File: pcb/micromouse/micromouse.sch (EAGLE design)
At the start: 55 parts, among them J1 Connector_M1, J2 Connector_M1, J4 Programmer, T1 2N3904

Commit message: Add correct switch, change connection of LEDs, connect signals from hbridge and motor with uC, fix connection of programmer, add signals to debugging pin header, add front wheel LED, connect capacitor to VCAP pin of uC.
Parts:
- removed LED3: green, led:LEDCHIP-LED0805
- removed ON/OFF: SWS001, smd-special:SWS001
- removed R2: ???, rcl:R-EU_R0805
- removed T1: 2N3904, transistor:2N3904
- added C17: 10uF, rcl:C-EUC0805
- added C18, C19, C20: 100nF, rcl:C-EUC0805
- added LED4: Front_wheel, led:LED5MM
- added S1: 1101M2S3CQE2, SamacSys_Parts:1101M2S3CQE2
- R1: value ??? -> 62
- R10, R11, R12: value 5.1 -> 121
- SV1: value (none) -> IR sensor 0
- SV2: value (none) -> IR sensor 1
- SV3: value (none) -> IR sensor 2
- SV4: value PIN header -> Pin header; device con-lstb:MA07-2 -> con-lstb:MA10-2
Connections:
- net AN0 renamed IR0
- net AN1 renamed IR1
- net AN4 renamed IR2
- removed net LED0: R10.2, R2.2
- removed net LED1: MICROCONTROLLER.PGED2/PWM1H3/RP10/CN16/PMD2/RB10, R11.2, SV4.14
- removed net LED2: MICROCONTROLLER.PGEC2/PWM1L3/RP11/CN15/PMD1/RB11, R12.2, SV4.12
- removed net LED3: MICROCONTROLLER.PWM1H2/DAC1RP/RP12/CN14/PMD0/RB12, SV4.10
- removed net MCLR: J4.1
- removed net N$11: R1.1, T1.C
- removed net N$13: LED3.C, R1.2
- removed net N$9: R2.1, T1.B
- removed net RP24: MICROCONTROLLER.RP24/CN20/PMA5/RC8
- removed net RP25: MICROCONTROLLER.RP25/CN19/PMA6/RC9
- new net IO0: MICROCONTROLLER.PWM1H1/RTCC/RP14/CN12/PMWR/RB14, SV4.9
- new net IO1: MICROCONTROLLER.SOSCO/T1CK/CN0/RA4, SV4.11
- new net IO2: MICROCONTROLLER.TDI/PMA9/RA9, SV4.13
- new net IO3: MICROCONTROLLER.RP21/CN26/PMA3/RC5, SV4.15
- new net IO4: MICROCONTROLLER.PGED3/ASDA1/RP5/CN27/PMD7/RB5, SV4.16
- new net N_LED0: LED0.C, MICROCONTROLLER.PGED2/PWM1H3/RP10/CN16/PMD2/RB10, SV4.14
- new net N_LED1: LED1.C, MICROCONTROLLER.PGEC2/PWM1L3/RP11/CN15/PMD1/RB11, SV4.12
- new net N_LED2: LED2.C, MICROCONTROLLER.PWM1H2/DAC1RP/RP12/CN14/PMD0/RB12, SV4.10
- new net VCAP/VDDCORE: C17.2, MICROCONTROLLER.VCAP/VDDCORE
- net +3V3: now also C18.2, C19.2, C20.2, J1.4, J2.4, R1.2, R10.2, R11.2, R12.2; no longer LED3.A
- net +5V: no longer J1.4, J2.4
- net +9V: now also S1.2, S1.3; no longer ON/OFF.2
- net ENC1_A: now also MICROCONTROLLER.RP24/CN20/PMA5/RC8
- net ENC1_B: now also MICROCONTROLLER.RP25/CN19/PMA6/RC9
- net ENC2_A: now also MICROCONTROLLER.RP19/CN28/PMBE/RC3
- net ENC2_B: now also MICROCONTROLLER.RP20/CN25/PMA4/RC4
- net GND: now also C17.1, C18.1, C19.1, C20.1, LED4.C; no longer LED0.C, LED1.C, LED2.C, T1.E
- net IO5: now also SV4.17; no longer SV4.3
- net IO6: now also SV4.18; no longer SV4.5
- net IO7: now also SV4.19; no longer SV4.9
- net IO8: now also SV4.20; no longer SV4.11
- net M1+_EN: now also MICROCONTROLLER.TMS/PMA10/RA10
- net M1-_EN: now also MICROCONTROLLER.TCK/PMA7/RA7
- net M2+_EN: now also MICROCONTROLLER.TDO/PMA8/RA8
- net M2-_EN: now also MICROCONTROLLER.SOSCI/RP4/CN1/RB4
- net N$2: now also LED4.A, R1.1; no longer SV4.13
- net N$3: now also S1.1; no longer ON/OFF.1
- net N_MCLR: now also J4.1
- net PGEC1: now also J4.5; no longer J4.4
- net PGED1: now also J4.4; no longer J4.5
- net RX: now also SV4.3
- net TX: now also SV4.5
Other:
- note added: "10mA @ 1.21 V"
- note added: "10mA @ 2.1 V"
- note added: "2.54mm grid needed according to motor data sheet (this conector fulfills this: https://www.mikrocontroller.net/topic/393245)"
- note added: "Add jumper to disconnect them from pins on uC in case we need the pins later on (like on demo board)? >>> No, we have enough pins on the board."
- note added: "IDEA: Should we use 3.3V instead since our digital logic is 3.3V as well? Worried that this wiill lead to 5V in the encoder output that then routes into the microcontroller. >>> Good point, cannot hurt."
- note added: "PIN6 EN nutzen? >>> Sehe jetzt keine Notwendigkeit. Das Setup mit den AT commands können wir ha auf dem Breadboard machen."
- note added: "TODO: @Ludwig Please check if the switch is connected as you intended it to be."
- note added: "TODO: Check if these are the correct ones. Seems to me that we need 1.5mm pin distances: https://www.datasheets.com/en/part-details/11501w00-3p-s-hf-r-shenglan-technology-co---ltd-403414635 Furthermore, female headers and not male headers are needed."
- note added: "TODO: Please check PGD and PGC. I think that PGD is on 4 and PGC on 5. >>> Yes, changed it. TODO 2: Why are on the demo board not the signals PGEC1 and PGED1 used but the outputs of pins 11 & 12?"
- note added: "TODO: S. 357 Microcontroller: Anscheinend haben unterschiedliche PINS unterschiedliche max. Strombegrenzung. Checken dass PINS 20mA liefern können. Zusätzlich 200mA max auf allen PINs. >>> Solution: Draw current diretly from power source (switching regulator)"
- note added: "TODO: Where do we need decoupling capacitors?"
- note removed: "(like on demo board)"
- note removed: "20mA @ 0.1 V?"
- note removed: "20mA @ 3.2 V?"
- note removed: "Add jumper to disconnect them from pins on uC in case we need the pins later on?"
- note removed: "Alternative: Transistor?"
- note removed: "IDEA: Add RX, TX"
- note removed: "IDEA: Should we use 3.3V instead since our digital logic is 3.3V as well? Worried that this wiill lead to 5V in the encoder output that then routes into the microcontroller"
- note removed: "PIN6 EN nutzen???? >>>Sehe jetzt keine Notwendigkeit. Das Setup mit den AT commands können wir ha auf dem Breadboard machen."
- note removed: "TODO: Check if these are the correct ones. Seems to me that we need 1.5mm pin distances: https://www.datasheets.com/en/part-details/11501w00-3p-s-hf-r-shenglan-technology-co---ltd-403414635"
- note removed: "TODO: Do we need decoupling capacitor?"
- note removed: "TODO: Find appropriate switch that matches excel sheet"
- note removed: "TODO: S. 357 Microcontroller: Anscheinend haben unterschiedliche PINS unterschiedliche max. Strombegrenzung. Checken dass PINS 20mA liefern können. Zusätzlich 200mA max auf allen PINs."
- note removed: "TOOD: Please check PGD and PGC. I think that PGD is on 4 and PGC on 5."
- note removed: "https://www.mikrocontroller.net/topic/393245 2.54mm grid"
- moved on the sheet: C8, J1, R1

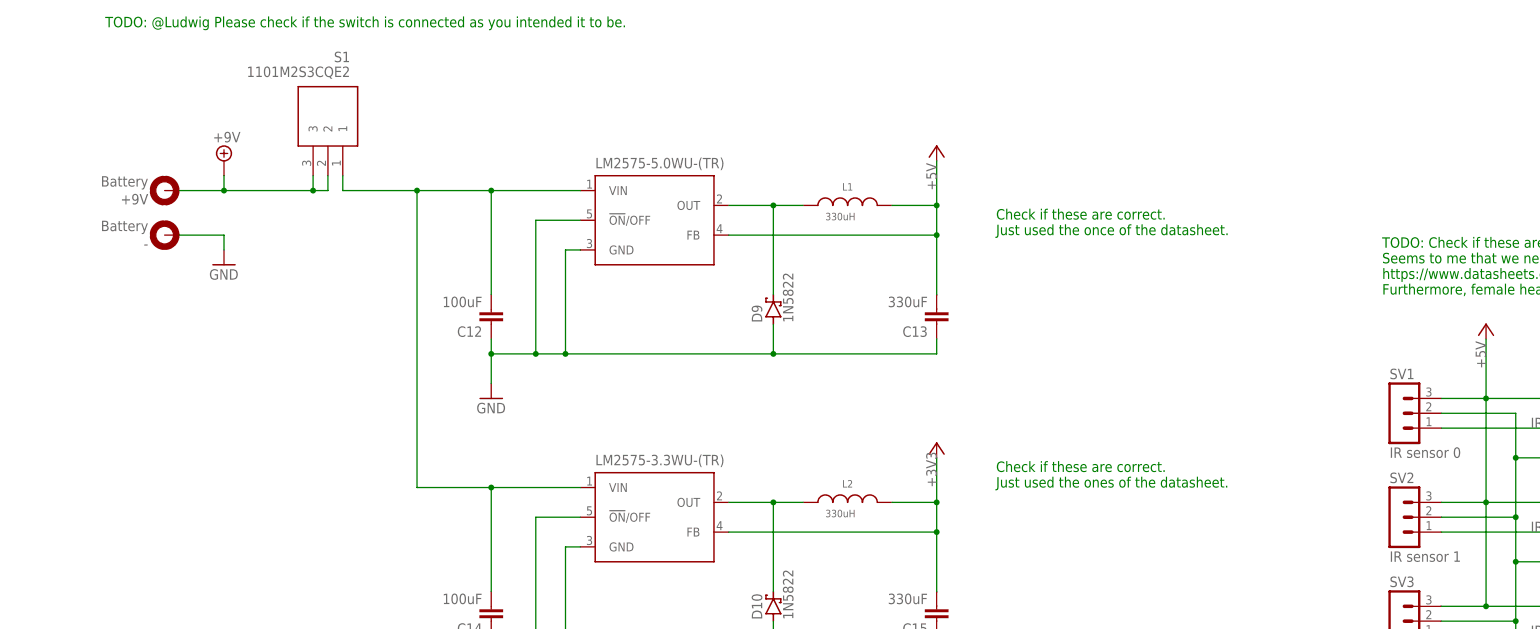
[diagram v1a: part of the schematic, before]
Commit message: Fixed connections of power switch and implemented inductors for voltage regulators
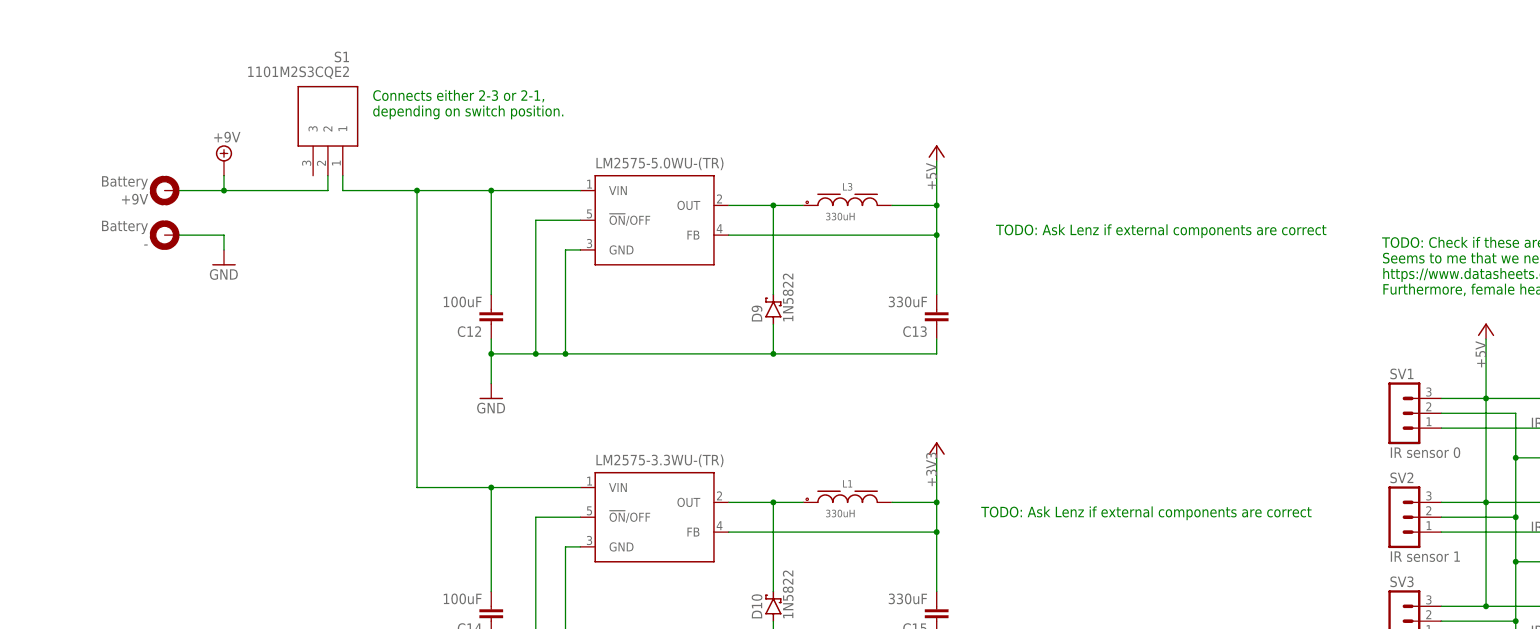
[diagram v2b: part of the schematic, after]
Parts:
- removed L2: 330uH, Eagle_WE-MK (rev21b):WE-MK_0805_7447880015_H0.85
- added L3: 330uH, Eagle_WE-PD (rev20a):WE-PD_1210_7447709331
- L1: device Eagle_WE-MK (rev21b):WE-MK_0805_7447880015_H0.85 -> Eagle_WE-PD (rev20a):WE-PD_1210_7447709331
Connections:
- net +3V3: now also L1.2; no longer L2.2
- net +5V: now also L3.2; no longer L1.2
- net +9V: no longer S1.3
- net N$7: now also L3.1; no longer L1.1
- net N$8: now also L1.1; no longer L2.1
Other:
- note added: "Connects either 2-3 or 2-1, depending on switch position."
- note added: "TODO: Ask Lenz if external components are correct"
- note removed: "Check if these are correct. Just used the once of the datasheet."
- note removed: "Check if these are correct. Just used the ones of the datasheet."
- note removed: "TODO: @Ludwig Please check if the switch is connected as you intended it to be."
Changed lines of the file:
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@@
 <part name="LM2575-5.0WU-(TR)" library="national-semiconductor" library_urn="urn:adsk.eagle:library:307" deviceset="LM2596" device="S" package3d_urn="urn:adsk.eagle:package:16438/2"/>
 <part name="C12" library="rcl" library_urn="urn:adsk.eagle:library:334" deviceset="C-EU" device="C0805" package3d_urn="urn:adsk.eagle:package:23617/2" value="100uF"/>
-<part name="L1" library="Eagle_WE-MK (rev21b)" deviceset="WE-MK_0805" device="_H0.85" package3d_urn="urn:adsk.eagle:package:28411842/3" technology="_7447880015" value="330uH"/>
 <part name="C13" library="rcl" library_urn="urn:adsk.eagle:library:334" deviceset="C-EU" device="C0805" package3d_urn="urn:adsk.eagle:package:23617/2" value="330uF"/>
 <part name="D9" library="diode" library_urn="urn:adsk.eagle:library:210" deviceset="BAT19" device="" package3d_urn="urn:adsk.eagle:package:43344/2" value="1N5822"/>
@@
 <part name="LM2575-3.3WU-(TR)" library="national-semiconductor" library_urn="urn:adsk.eagle:library:307" deviceset="LM2596" device="S" package3d_urn="urn:adsk.eagle:package:16438/2"/>
 <part name="C14" library="rcl" library_urn="urn:adsk.eagle:library:334" deviceset="C-EU" device="C0805" package3d_urn="urn:adsk.eagle:package:23617/2" value="100uF"/>
-<part name="L2" library="Eagle_WE-MK (rev21b)" deviceset="WE-MK_0805" device="_H0.85" package3d_urn="urn:adsk.eagle:package:28411842/3" technology="_7447880015" value="330uH"/>
 <part name="C15" library="rcl" library_urn="urn:adsk.eagle:library:334" deviceset="C-EU" device="C0805" package3d_urn="urn:adsk.eagle:package:23617/2" value="330uF"/>
 <part name="D10" library="diode" library_urn="urn:adsk.eagle:library:210" deviceset="BAT19" device="" package3d_urn="urn:adsk.eagle:package:43344/2" value="1N5822"/>
@@
 <part name="C20" library="rcl" library_urn="urn:adsk.eagle:library:334" deviceset="C-EU" device="C0805" package3d_urn="urn:adsk.eagle:package:23617/2" value="100nF"/>
 <part name="S1" library="SamacSys_Parts" deviceset="1101M2S3CQE2" device=""/>
+<part name="L3" library="Eagle_WE-PD (rev20a)" deviceset="WE-PD_1210" device="" package3d_urn="urn:adsk.eagle:package:13009201/2" technology="_7447709331" value="330uH"/>
+<part name="L1" library="Eagle_WE-PD (rev20a)" deviceset="WE-PD_1210" device="" package3d_urn="urn:adsk.eagle:package:13009201/2" technology="_7447709331" value="330uH"/>
 </parts>
 <sheets>
@@
 instead of soldering the chip directly onto the board</text>
 <text x="157.48" y="58.42" size="1.778" layer="91">f_cutoff = 796Hz, same as on dev board</text>
-<text x="35.56" y="337.82" size="1.778" layer="91">Check if these are correct.
-Just used the once of the datasheet.</text>
-<text x="35.56" y="294.64" size="1.778" layer="91">Check if these are correct.
-Just used the ones of the datasheet.</text>
+<text x="35.56" y="337.82" size="1.778" layer="91">TODO: Ask Lenz if external components are correct</text>
 <text x="119.38" y="220.98" size="1.778" layer="91">TODO: Please check PGD and PGC.
 I think that PGD is on 4 and PGC on 5.
@@
 https://www.datasheets.com/en/part-details/11501w00-3p-s-hf-r-shenglan-technology-co---ltd-403414635
 Furthermore, female headers and not male headers are needed.</text>
-<text x="-116.84" y="373.38" size="1.778" layer="91">TODO: @Ludwig Please check if the switch is connected as you intended it to be.</text>
+<text x="-71.12" y="358.14" size="1.778" layer="91">Connects either 2-3 or 2-1,
+depending on switch position.</text>
+<text x="33.02" y="289.56" size="1.778" layer="91">TODO: Ask Lenz if external components are correct</text>
 </plain>
 <instances>
@@
 <attribute name="VALUE" x="-52.324" y="327.279" size="1.778" layer="96" rot="R180"/>
 </instance>
-<instance part="L1" gate="G$1" x="10.16" y="342.9" smashed="yes">
-<attribute name="NAME" x="10.16" y="345.44" size="1.27" layer="95" align="bottom-center"/>
-<attribute name="VALUE" x="6.35" y="340.36" size="1.27" layer="96"/>
-</instance>
 <instance part="C13" gate="G$1" x="25.4" y="322.58" smashed="yes" rot="R180">
 <attribute name="NAME" x="23.876" y="322.199" size="1.778" layer="95" rot="R180"/>
@@
 <attribute name="VALUE" x="-52.324" y="276.479" size="1.778" layer="96" rot="R180"/>
 </instance>
-<instance part="L2" gate="G$1" x="10.16" y="292.1" smashed="yes">
-<attribute name="NAME" x="10.16" y="294.64" size="1.27" layer="95" align="bottom-center"/>
-<attribute name="VALUE" x="6.35" y="289.56" size="1.27" layer="96"/>
-</instance>
 <instance part="C15" gate="G$1" x="25.4" y="271.78" smashed="yes" rot="R180">
 <attribute name="NAME" x="23.876" y="271.399" size="1.778" layer="95" rot="R180"/>
@@
 <attribute name="NAME" x="-74.93" y="368.3" size="1.778" layer="95" rot="R180" align="center-left"/>
 <attribute name="VALUE" x="-74.93" y="365.76" size="1.778" layer="96" rot="R180" align="center-left"/>
+</instance>
+<instance part="L3" gate="G$1" x="10.16" y="342.9" smashed="yes">
+<attribute name="NAME" x="10.16" y="345.44" size="1.27" layer="95" align="bottom-center"/>
+<attribute name="VALUE" x="6.35" y="340.36" size="1.27" layer="96"/>
+</instance>
+<instance part="L1" gate="G$1" x="10.16" y="292.1" smashed="yes">
+<attribute name="NAME" x="10.16" y="294.64" size="1.27" layer="95" align="bottom-center"/>
+<attribute name="VALUE" x="6.35" y="289.56" size="1.27" layer="96"/>
 </instance>
 </instances>
@@
 </segment>
 <segment>
-<pinref part="L2" gate="G$1" pin="2"/>
 <wire x1="17.78" y1="292.1" x2="25.4" y2="292.1" width="0.1524" layer="91"/>
 <pinref part="C15" gate="G$1" pin="2"/>
@@
 <wire x1="25.4" y1="299.72" x2="25.4" y2="292.1" width="0.1524" layer="91"/>
 <pinref part="+3V4" gate="G$1" pin="+3V3"/>
+<pinref part="L1" gate="G$1" pin="2"/>
 </segment>
 <segment>
@@
 </segment>
 <segment>
-<pinref part="L1" gate="G$1" pin="2"/>
 <wire x1="17.78" y1="342.9" x2="25.4" y2="342.9" width="0.1524" layer="91"/>
 <pinref part="C13" gate="G$1" pin="2"/>
@@
 <pinref part="P+3" gate="1" pin="+5V"/>
 <wire x1="25.4" y1="350.52" x2="25.4" y2="342.9" width="0.1524" layer="91"/>
+<pinref part="L3" gate="G$1" pin="2"/>
 </segment>
 <segment>
@@
 <pinref part="SUPPLY1" gate="G$1" pin="+9V"/>
 <wire x1="-96.52" y1="345.44" x2="-96.52" y2="347.98" width="0.1524" layer="91"/>
-<wire x1="-78.74" y1="345.44" x2="-81.28" y2="345.44" width="0.1524" layer="91"/>
 <pinref part="+9V" gate="G$1" pin="MOUNT"/>
-<wire x1="-81.28" y1="345.44" x2="-96.52" y2="345.44" width="0.1524" layer="91"/>
 <wire x1="-104.14" y1="345.44" x2="-96.52" y2="345.44" width="0.1524" layer="91"/>
+<wire x1="-96.52" y1="345.44" x2="-78.74" y2="345.44" width="0.1524" layer="91"/>
 <junction x="-96.52" y="345.44"/>
 <pinref part="S1" gate="G$1" pin="2"/>
 <wire x1="-78.74" y1="345.44" x2="-78.74" y2="347.98" width="0.1524" layer="91"/>
-<pinref part="S1" gate="G$1" pin="3"/>
-<wire x1="-81.28" y1="347.98" x2="-81.28" y2="345.44" width="0.1524" layer="91"/>
-<junction x="-81.28" y="345.44"/>
 </segment>
 <segment>
@@
 <segment>
 <pinref part="LM2575-5.0WU-(TR)" gate="G$1" pin="OUT"/>
-<pinref part="L1" gate="G$1" pin="1"/>
 <wire x1="-10.16" y1="342.9" x2="-2.54" y2="342.9" width="0.1524" layer="91"/>
 <pinref part="D9" gate="1" pin="C"/>
@@
 <wire x1="-2.54" y1="327.66" x2="-2.54" y2="342.9" width="0.1524" layer="91"/>
 <junction x="-2.54" y="342.9"/>
+<pinref part="L3" gate="G$1" pin="1"/>
 </segment>
 </net>
@@
 <segment>
 <pinref part="LM2575-3.3WU-(TR)" gate="G$1" pin="OUT"/>
-<pinref part="L2" gate="G$1" pin="1"/>
 <wire x1="-10.16" y1="292.1" x2="-2.54" y2="292.1" width="0.1524" layer="91"/>
 <pinref part="D10" gate="1" pin="C"/>
@@
 <wire x1="-2.54" y1="276.86" x2="-2.54" y2="292.1" width="0.1524" layer="91"/>
 <junction x="-2.54" y="292.1"/>
+<pinref part="L1" gate="G$1" pin="1"/>
 </segment>
 </net>
@@
 <junction x="-50.8" y="294.64"/>
 <wire x1="-63.5" y1="345.44" x2="-63.5" y2="294.64" width="0.1524" layer="91"/>
+<pinref part="S1" gate="G$1" pin="1"/>
+<wire x1="-76.2" y1="347.98" x2="-76.2" y2="345.44" width="0.1524" layer="91"/>
 <wire x1="-76.2" y1="345.44" x2="-63.5" y2="345.44" width="0.1524" layer="91"/>
 <junction x="-63.5" y="345.44"/>
-<pinref part="S1" gate="G$1" pin="1"/>
-<wire x1="-76.2" y1="347.98" x2="-76.2" y2="345.44" width="0.1524" layer="91"/>
-</segment>
-</net>
+</segment>
+</net>
